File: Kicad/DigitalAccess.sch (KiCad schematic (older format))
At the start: 11 parts, among them U2 MCP3901, X1 CRYSTAL

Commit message: updated based on feedback. Ready for second review
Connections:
- net pH_ADC+: now also U2.5 (CH0-); no longer U2.4 (CH0+)
- net pH_ADC-: now also U2.4 (CH0+); no longer U2.5 (CH0-)
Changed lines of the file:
@@
 $Descr A4 11693 8268
 encoding utf-8
-Sheet 7 7
+Sheet 6 7
 Title ""
-Date "18 oct 2014"
+Date "21 oct 2014"
 Rev ""
 Comp ""
@@
 ~DR
 $Comp
-L AGND #PWR010
+L AGND #PWR012
 U 1 1 527EEF67
 P 6100 4700
-F 0 "#PWR010" H 6100 4700 40  0001 C CNN
+F 0 "#PWR012" H 6100 4700 40  0001 C CNN
 F 1 "AGND" H 6100 4630 50  0000 C CNN
 F 2 "~" H 6100 4700 60  0000 C CNN
@@
 $EndComp
 $Comp
-L AGND #PWR011
+L AGND #PWR013
 U 1 1 527EEF6D
 P 5300 4700
-F 0 "#PWR011" H 5300 4700 40  0001 C CNN
+F 0 "#PWR013" H 5300 4700 40  0001 C CNN
 F 1 "AGND" H 5300 4630 50  0000 C CNN
 F 2 "~" H 5300 4700 60  0000 C CNN
@@
 $EndComp
 $Comp
-L AGND #PWR012
+L AGND #PWR014
 U 1 1 527EEF73
 P 4750 1500
-F 0 "#PWR012" H 4750 1500 40  0001 C CNN
+F 0 "#PWR014" H 4750 1500 40  0001 C CNN
 F 1 "AGND" H 4750 1430 50  0000 C CNN
 F 2 "~" H 4750 1500 60  0000 C CNN
@@
 $EndComp
 $Comp
-L AGND #PWR013
+L AGND #PWR015
 U 1 1 527EEF79
 P 7200 1700
-F 0 "#PWR013" H 7200 1700 40  0001 C CNN
+F 0 "#PWR015" H 7200 1700 40  0001 C CNN
 F 1 "AGND" H 7200 1630 50  0000 C CNN
 F 2 "~" H 7200 1700 60  0000 C CNN
@@
 $EndComp
 $Comp
-L AGND #PWR014
+L AGND #PWR016
 U 1 1 53CD7905
 P 3750 2250
-F 0 "#PWR014" H 3750 2250 40  0001 C CNN
+F 0 "#PWR016" H 3750 2250 40  0001 C CNN
 F 1 "AGND" H 3750 2180 50  0000 C CNN
 F 2 "~" H 3750 2250 60  0000 C CNN
@@
 	-1   0    0    1
 $EndComp
+Text HLabel 7900 3250 2    60   Input ~ 0
+pH_ADC+
 Text HLabel 7900 3150 2    60   Input ~ 0
-pH_ADC+
-Text HLabel 7900 3250 2    60   Input ~ 0
 pH_ADC-
 $Comp
@@
 Connection ~ 3550 2200
 Wire Wire Line
+	7250 3250 7900 3250
+Wire Wire Line
 	7250 3150 7900 3150
-Wire Wire Line
-	7250 3250 7900 3250
 Wire Wire Line
 	3200 2450 3200 2700
@@
 	8450 2900 8450 2800
 $Comp
-L AGND #PWR015
+L AGND #PWR017
 U 1 1 53E3E82B
 P 8300 3000
-F 0 "#PWR015" H 8300 3000 40  0001 C CNN
+F 0 "#PWR017" H 8300 3000 40  0001 C CNN
 F 1 "AGND" H 8300 2930 50  0000 C CNN
 F 2 "~" H 8300 3000 60  0000 C CNN
@@
 	7450 2450 7450 2650
 $Comp
-L AGND #PWR016
+L AGND #PWR018
 U 1 1 53F231BC
 P 7450 2650
-F 0 "#PWR016" H 7450 2650 40  0001 C CNN
+F 0 "#PWR018" H 7450 2650 40  0001 C CNN
 F 1 "AGND" H 7450 2580 50  0000 C CNN
 F 2 "" H 7450 2650 60  0000 C CNN

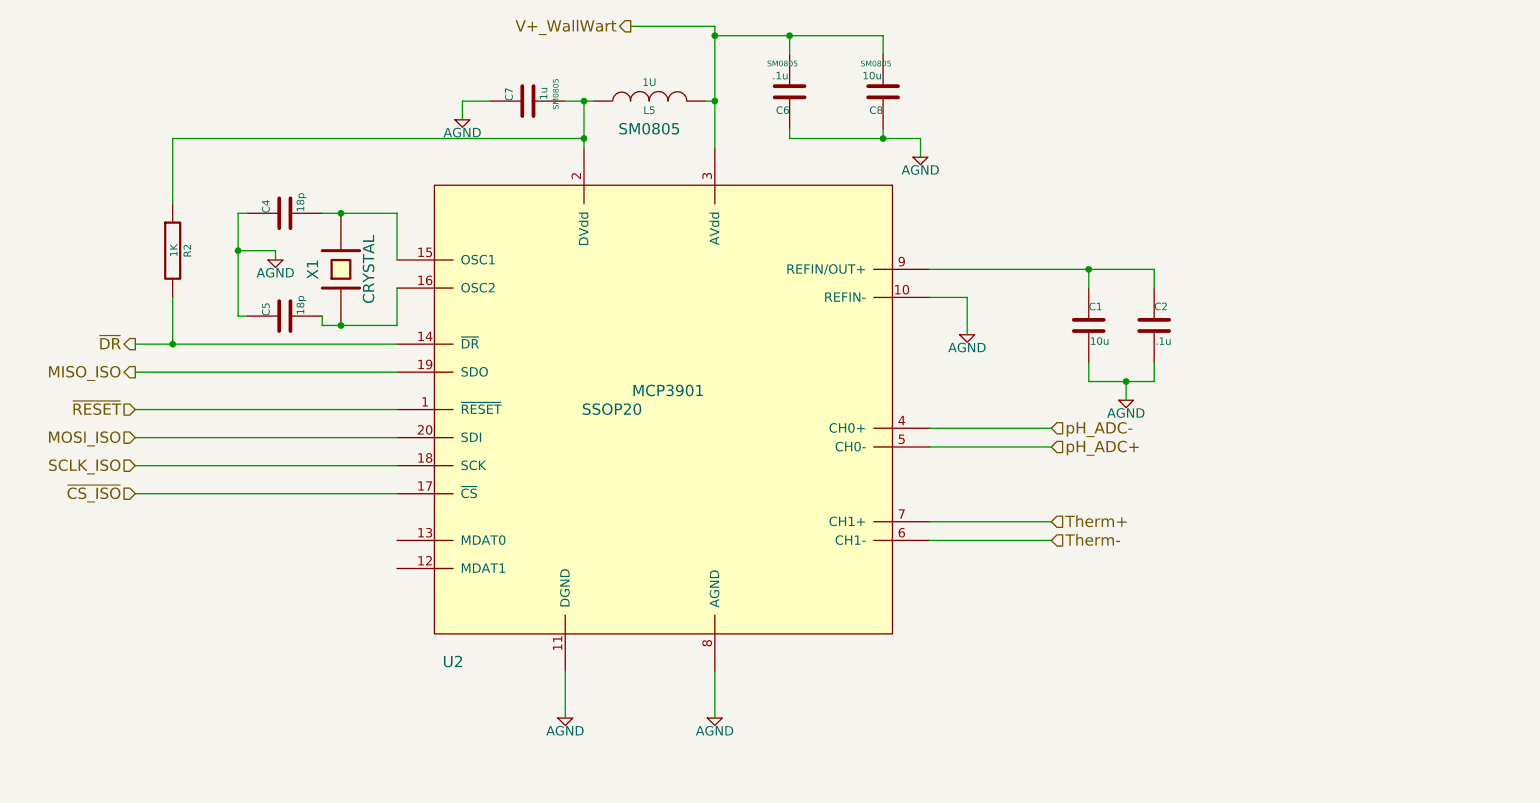
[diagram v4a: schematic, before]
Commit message: first pass changing ADC
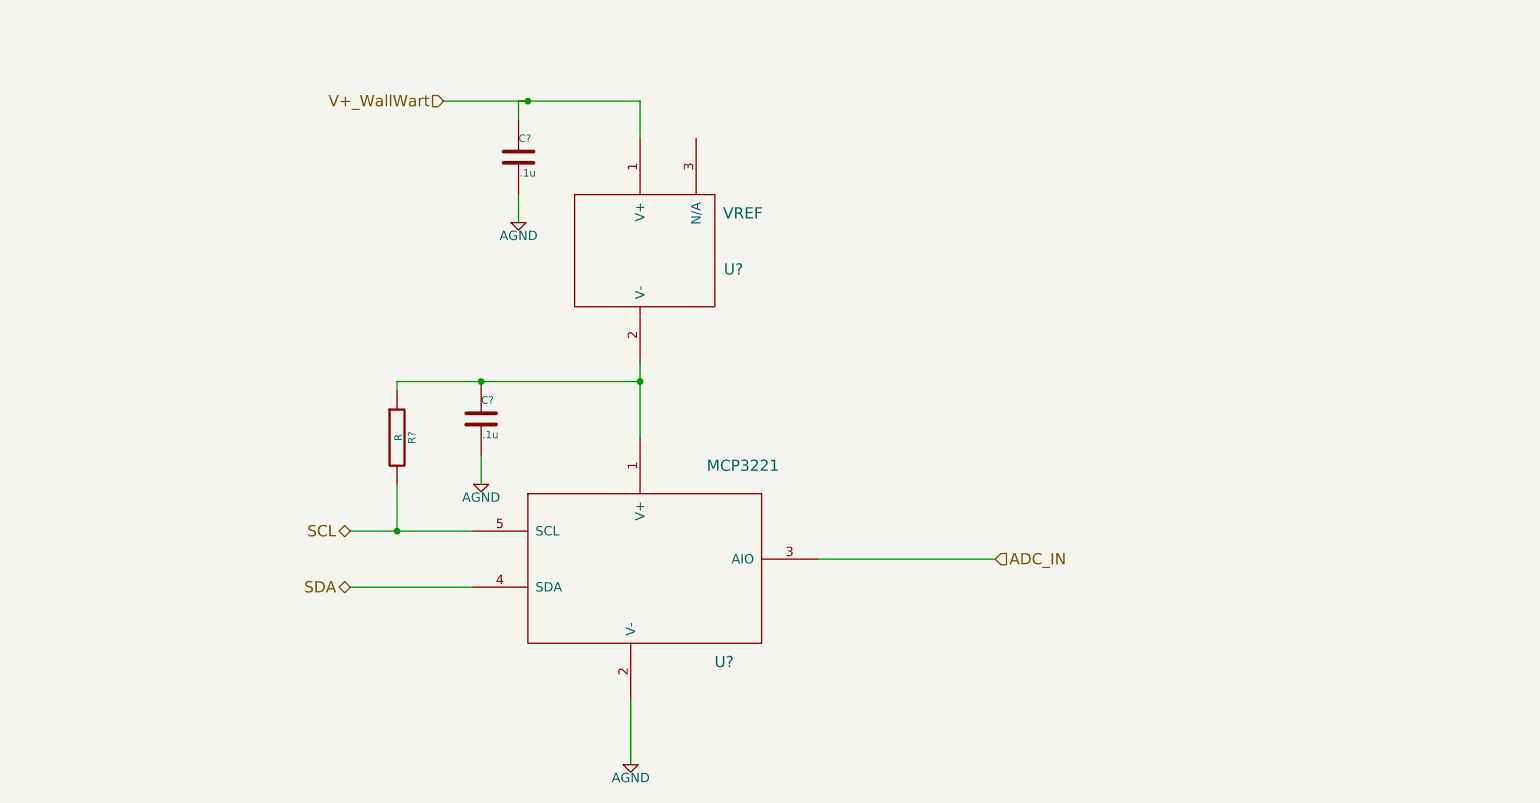
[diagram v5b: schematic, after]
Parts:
- removed C1: 10u, ~, symbol C
- removed C2: .1u, ~, symbol C
- removed C4, C5: 18p, ~, symbol C
- removed C6: .1u, SM0805, symbol C
- removed C7: 1u, SM0805, symbol C
- removed C8: 10u, SM0805, symbol C
- removed L5: 1U, SM0805, symbol INDUCTOR
- removed R2: 1K, ~, symbol R
- removed U2: MCP3901, SSOP20, symbol MCP3901
- removed X1: CRYSTAL, ~, symbol CRYSTAL
- added C? (x2): .1u, ~, symbol C
- added R?: R, ~, symbol R
- added U?: VREF, symbol VREF
- added U?: MCP3221, ~, symbol MCP3221
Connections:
- net AGND: now also C?.2, C?.2, U?.2 (V-)
- net V+_WallWart: now also C?.1, U?.1 (V+)
- new net: C?.1, R?.1, U?.1 (V+), U?.2 (V-)
- new net ADC_IN: U?.3 (AIO)
- new net SCL: R?.2, U?.5 (SCL)
- new net SDA: U?.4 (SDA)

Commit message: prior to using Arduino ADC
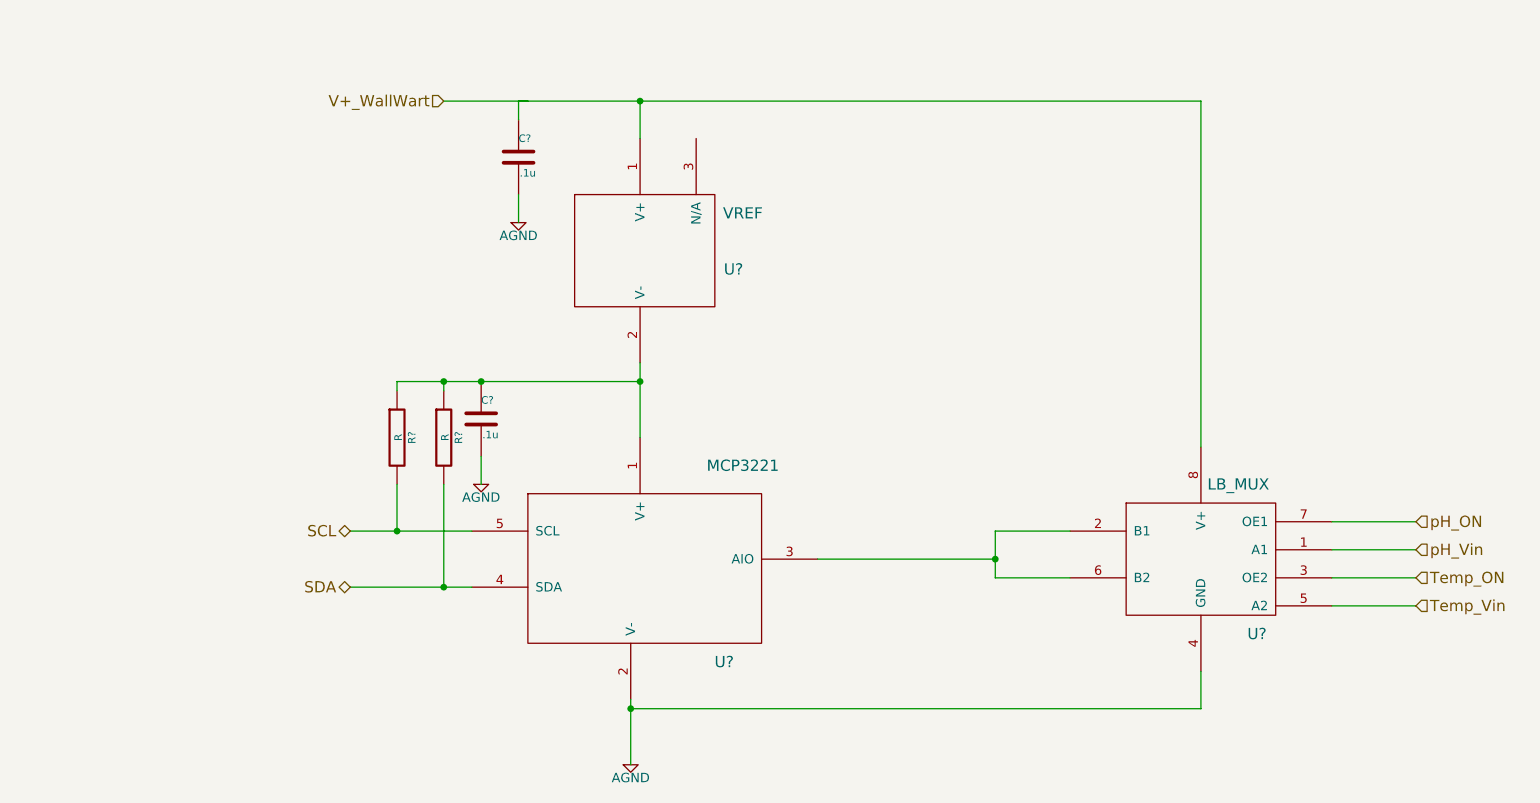
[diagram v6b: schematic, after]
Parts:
- added R?: R, ~, symbol R
- added U?: LB_MUX, symbol LB_MUX
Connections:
- net labels added: Temp_ON, Temp_Vin, pH_ON, pH_Vin
- net labels removed: ADC_IN
- wire segments 14 -> 26
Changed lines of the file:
@@
 $Descr A4 11693 8268
 encoding utf-8
-Sheet 7 7
+Sheet 6 7
 Title ""
-Date "11 nov 2014"
+Date "12 nov 2014"
 Rev ""
 Comp ""
@@
 Wire Wire Line
 	4800 4000 4150 4000
-Text HLabel 7600 3850 2    60   Input ~ 0
-ADC_IN
 $Comp
 L MCP3221 U?
@@
 $EndComp
 Wire Wire Line
-	5700 1400 5050 1400
+	5050 1400 8700 1400
 Wire Wire Line
 	5050 1400 5050 1500
 Wire Wire Line
 	4650 1400 5100 1400
-Connection ~ 5100 1400
 $Comp
 L AGND #PWR?
@@
 	4400 3450 4400 3700
 Connection ~ 4400 3700
+$Comp
+L R R?
+U 1 1 546247DE
+P 4650 3200
+F 0 "R?" V 4730 3200 40  0000 C CNN
+F 1 "R" V 4657 3201 40  0000 C CNN
+F 2 "~" V 4580 3200 30  0000 C CNN
+F 3 "~" H 4650 3200 30  0000 C CNN
+	1    4650 3200
+	1    0    0    -1
+$EndComp
+Wire Wire Line
+	4650 2950 4650 2900
+Connection ~ 4650 2900
+Wire Wire Line
+	4650 3450 4650 4000
+Connection ~ 4650 4000
+$Comp
+L LB_MUX U?
+U 1 1 54637A95
+P 8700 3850
+F 0 "U?" H 9000 3450 60  0000 C CNN
+F 1 "LB_MUX" H 8900 4250 60  0000 C CNN
+F 2 "" H 8700 3850 60  0000 C CNN
+F 3 "" H 8700 3850 60  0000 C CNN
+	1    8700 3850
+	1    0    0    -1
+$EndComp
+Wire Wire Line
+	8000 3700 7600 3700
+Wire Wire Line
+	7600 3700 7600 3950
+Wire Wire Line
+	7600 3950 8000 3950
+Connection ~ 7600 3850
+Wire Wire Line
+	8700 4650 5650 4650
+Connection ~ 5650 4650
+Wire Wire Line
+	8700 4450 8700 4650
+Wire Wire Line
+	8700 1400 8700 3250
+Connection ~ 5700 1400
+Text HLabel 9850 3800 2    60   Input ~ 0
+pH_Vin
+Wire Wire Line
+	9850 3800 9400 3800
+Text HLabel 9850 4100 2    60   Input ~ 0
+Temp_Vin
+Wire Wire Line
+	9850 4100 9400 4100
+Text HLabel 9850 3650 2    60   Input ~ 0
+pH_ON
+Wire Wire Line
+	9400 3650 9850 3650
+Text HLabel 9850 3950 2    60   Input ~ 0
+Temp_ON
+Wire Wire Line
+	9400 3950 9850 3950
 $EndSCHEMATC

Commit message: changed to mcp3221 - not complete
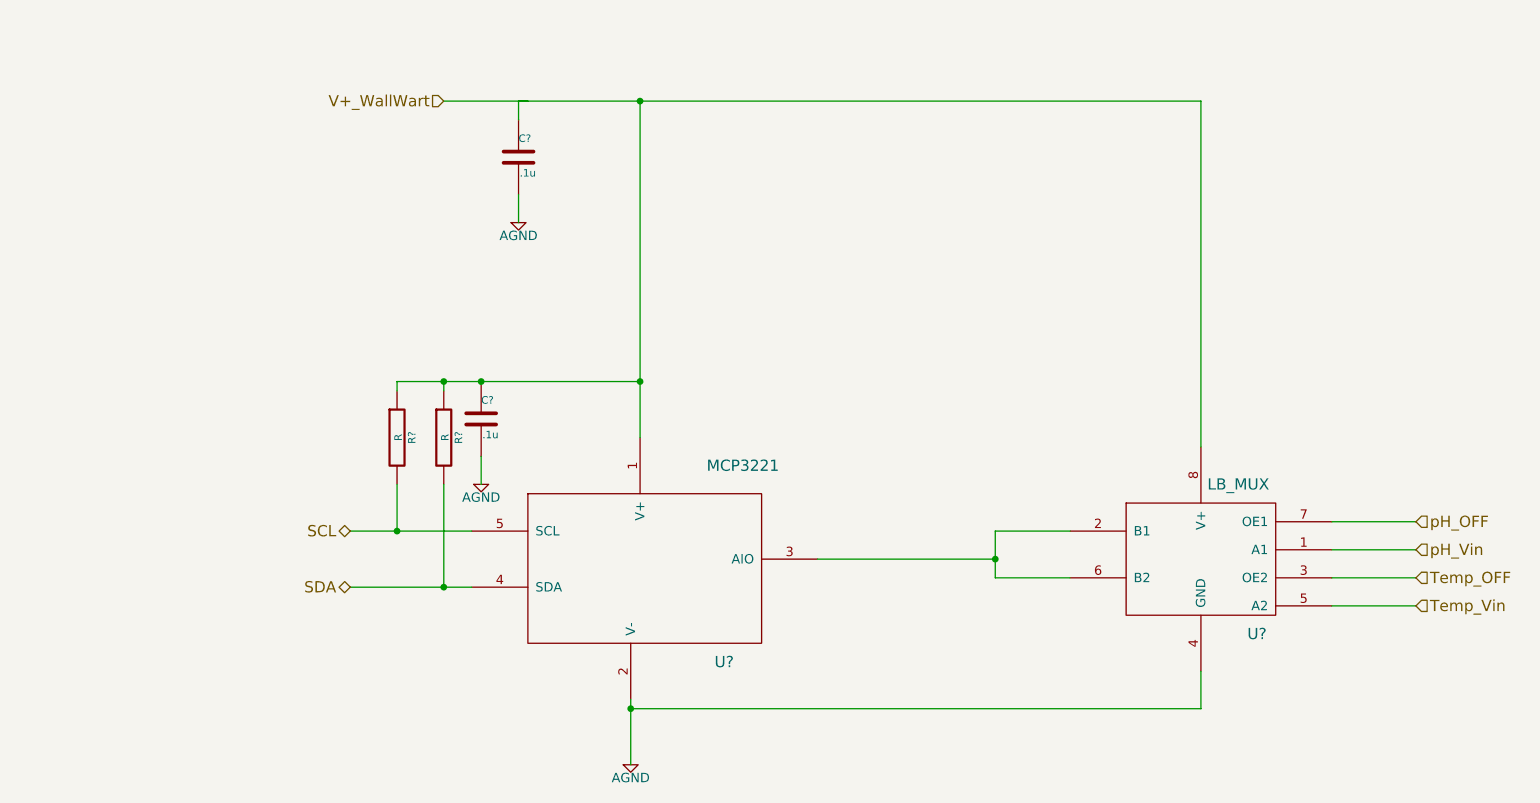
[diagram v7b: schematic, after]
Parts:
- removed U?: VREF, symbol VREF
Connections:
- net labels added: Temp_OFF, pH_OFF
- net labels removed: Temp_ON, pH_ON
- wire segments 26 -> 25
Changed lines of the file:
@@
 Sheet 6 7
 Title ""
-Date "12 nov 2014"
+Date "25 nov 2014"
 Rev ""
 Comp ""
@@
 	1    0    0    -1
 $EndComp
-$Comp
-L VREF U?
-U 1 1 5461FB75
-P 5700 2150
-F 0 "U?" H 6200 2000 60  0000 C CNN
-F 1 "VREF" H 6250 2300 60  0000 C CNN
-F 2 "" H 5450 2250 60  0000 C CNN
-F 3 "" H 5450 2250 60  0000 C CNN
-	1    5700 2150
-	1    0    0    -1
-$EndComp
 Text HLabel 4650 1400 0    60   Input ~ 0
 V+_WallWart
 Wire Wire Line
-	5700 1400 5700 1600
-Wire Wire Line
-	5700 3200 5700 2800
+	5700 1400 5700 3200
 Text HLabel 4150 3700 0    60   BiDi ~ 0
 SCL
@@
 SDA
 Wire Wire Line
-	4800 4000 4150 4000
+	4150 4000 4800 4000
 $Comp
 L MCP3221 U?
@@
 	1    0    0    -1
 $EndComp
-Wire Wire Line
-	5050 1400 8700 1400
 Wire Wire Line
 	5050 1400 5050 1500
@@
 Wire Wire Line
 	8700 1400 8700 3250
-Connection ~ 5700 1400
 Text HLabel 9850 3800 2    60   Input ~ 0
 pH_Vin
@@
 	9850 4100 9400 4100
 Text HLabel 9850 3650 2    60   Input ~ 0
-pH_ON
+pH_OFF
 Wire Wire Line
 	9400 3650 9850 3650
 Text HLabel 9850 3950 2    60   Input ~ 0
-Temp_ON
+Temp_OFF
 Wire Wire Line
 	9400 3950 9850 3950
+Wire Wire Line
+	5050 1400 8700 1400
+Connection ~ 5700 1400
 $EndSCHEMATC
